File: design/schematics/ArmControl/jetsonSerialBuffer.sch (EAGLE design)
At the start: 7 parts, among them T1 2N3904, T2 2N3904

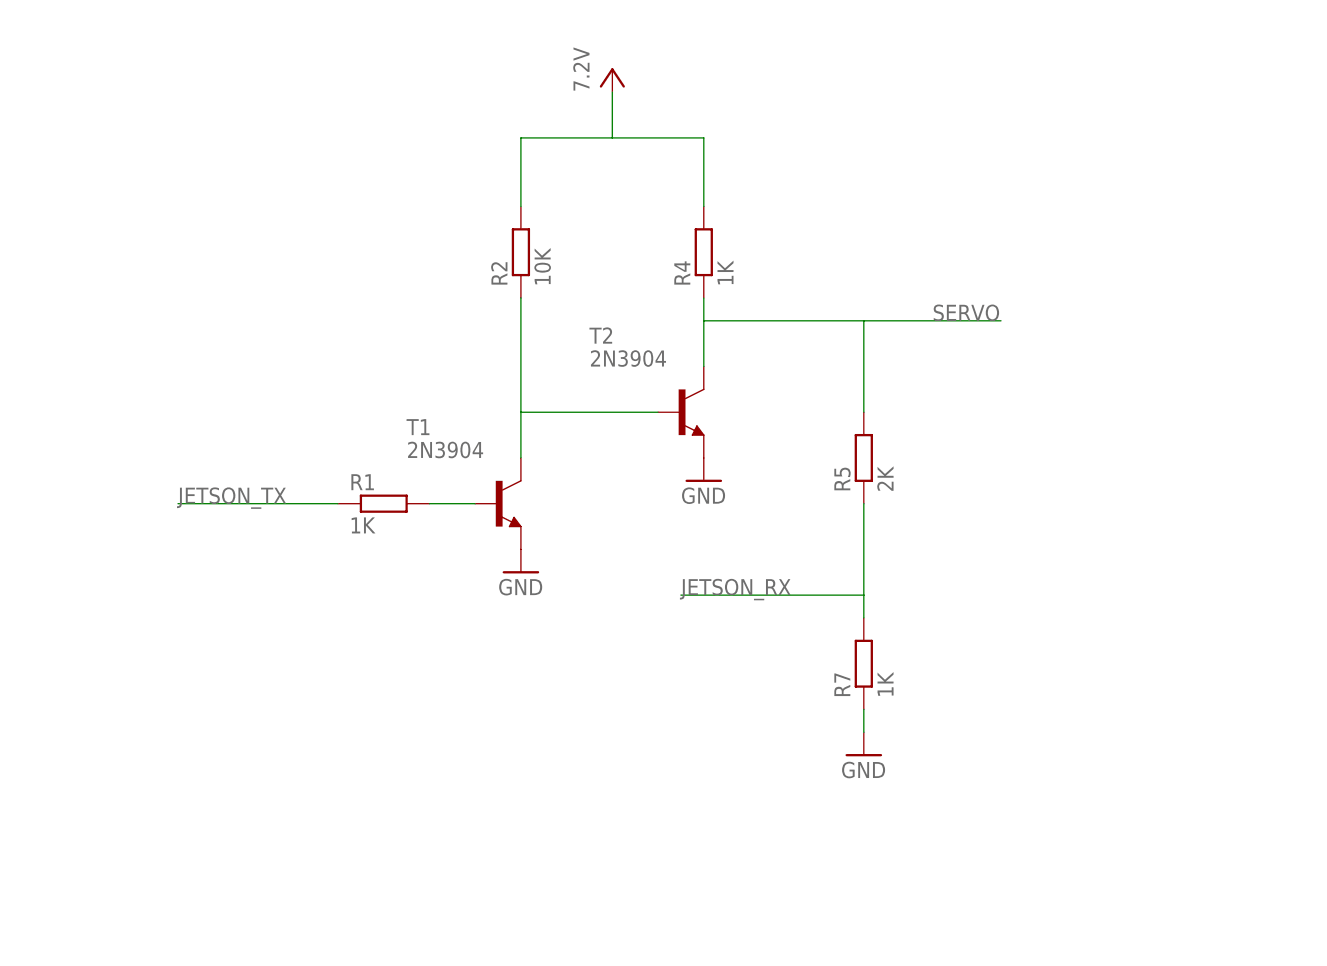
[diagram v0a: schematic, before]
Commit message: updated repo to match current impl
added schematics and pictures
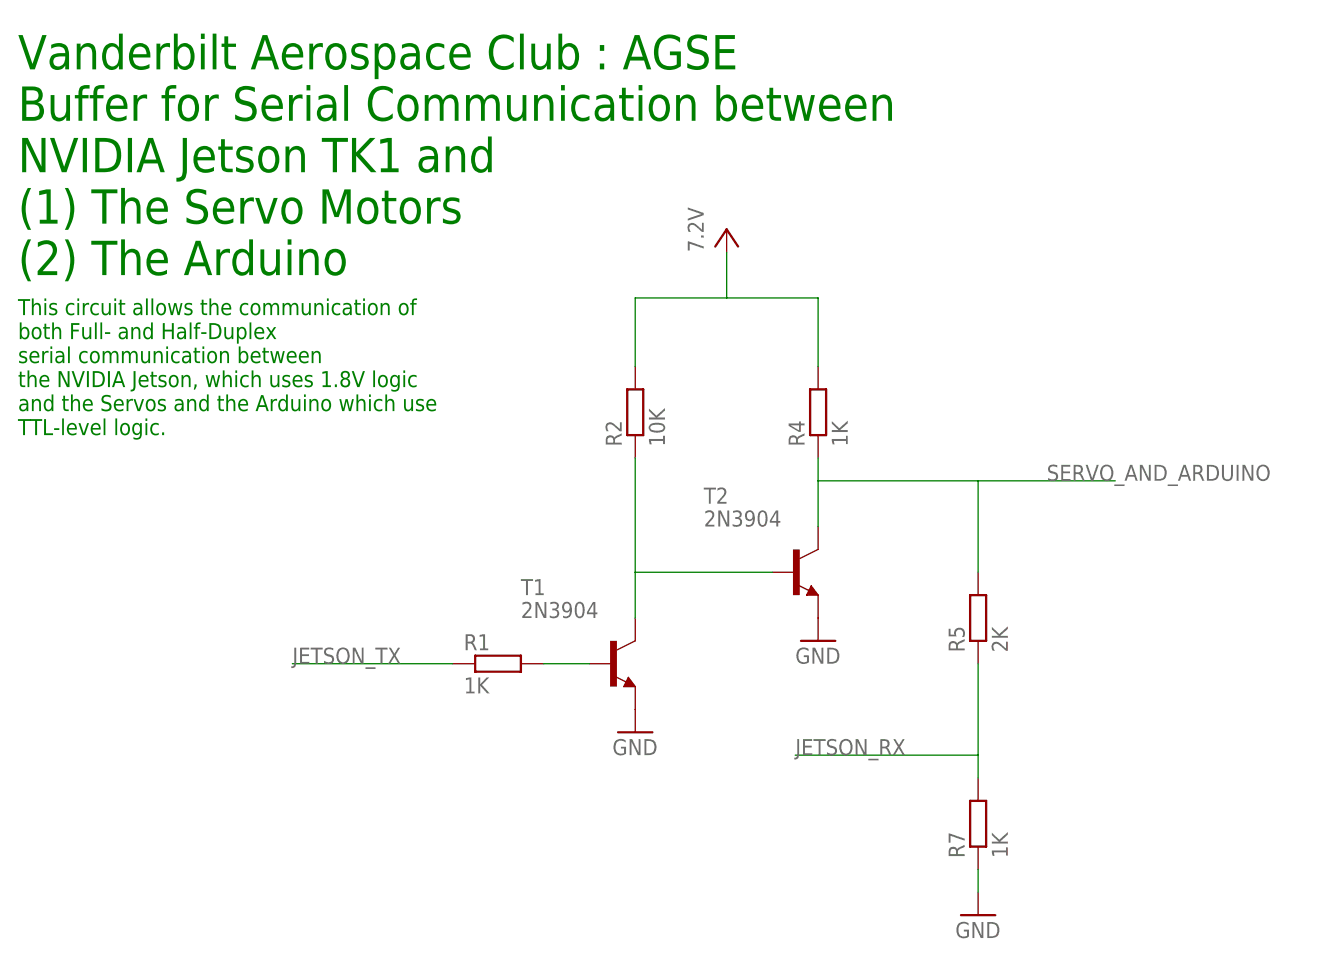
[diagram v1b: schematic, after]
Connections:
- net SERVO renamed SERVO_AND_ARDUINO
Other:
- note added: "This circuit allows the communication of both Full- and Half-Duplex serial communication between the NVIDIA Jetson, which uses 1.8V logic and the Servos and the Arduino which use TTL-level logic."
- note added: "Vanderbilt Aerospace Club : AGSE Buffer for Serial Communication between NVIDIA Jetson TK1 and (1) The Servo Motors (2) The Arduino"
- moved on the sheet: R1, R2, R4, R5, R7, T1, T2
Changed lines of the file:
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@@
 <sheet>
 <plain>
+<text x="10.16" y="99.06" size="3.81" layer="91">Vanderbilt Aerospace Club : AGSE
+Buffer for Serial Communication between
+NVIDIA Jetson TK1 and
+(1) The Servo Motors
+(2) The Arduino</text>
+<text x="10.16" y="81.28" size="1.778" layer="91">This circuit allows the communication of
+both Full- and Half-Duplex
+serial communication between
+the NVIDIA Jetson, which uses 1.8V logic
+and the Servos and the Arduino which use
+TTL-level logic.</text>
 </plain>
 <instances>
-<instance part="T1" gate="G1" x="63.5" y="73.66"/>
-<instance part="T2" gate="G1" x="83.82" y="83.82"/>
-<instance part="R1" gate="G$1" x="50.8" y="73.66"/>
-<instance part="GND1" gate="1" x="66.04" y="66.04"/>
-<instance part="P+1" gate="VCC" x="76.2" y="121.92"/>
-<instance part="R2" gate="G$1" x="66.04" y="101.6" rot="R90"/>
-<instance part="R4" gate="G$1" x="86.36" y="101.6" rot="R90"/>
-<instance part="R5" gate="G$1" x="104.14" y="78.74" rot="R90"/>
-<instance part="R7" gate="G$1" x="104.14" y="55.88" rot="R90"/>
-<instance part="GND3" gate="1" x="86.36" y="76.2"/>
-<instance part="GND4" gate="1" x="104.14" y="45.72"/>
+<instance part="T1" gate="G1" x="76.2" y="55.88"/>
+<instance part="T2" gate="G1" x="96.52" y="66.04"/>
+<instance part="R1" gate="G$1" x="63.5" y="55.88"/>
+<instance part="GND1" gate="1" x="78.74" y="48.26"/>
+<instance part="P+1" gate="VCC" x="88.9" y="104.14"/>
+<instance part="R2" gate="G$1" x="78.74" y="83.82" rot="R90"/>
+<instance part="R4" gate="G$1" x="99.06" y="83.82" rot="R90"/>
+<instance part="R5" gate="G$1" x="116.84" y="60.96" rot="R90"/>
+<instance part="R7" gate="G$1" x="116.84" y="38.1" rot="R90"/>
+<instance part="GND3" gate="1" x="99.06" y="58.42"/>
+<instance part="GND4" gate="1" x="116.84" y="27.94"/>
 <instance part="FRAME2" gate="G$1" x="0" y="0"/>
 </instances>
@@
 <pinref part="T1" gate="G1" pin="B"/>
 <pinref part="R1" gate="G$1" pin="2"/>
-<wire x1="55.88" y1="73.66" x2="60.96" y2="73.66" width="0.1524" layer="91"/>
+<wire x1="68.58" y1="55.88" x2="73.66" y2="55.88" width="0.1524" layer="91"/>
 </segment>
 </net>
@@
 <pinref part="R7" gate="G$1" pin="1"/>
 <pinref part="GND4" gate="1" pin="GND"/>
-<wire x1="104.14" y1="48.26" x2="104.14" y2="50.8" width="0.1524" layer="91"/>
+<wire x1="116.84" y1="30.48" x2="116.84" y2="33.02" width="0.1524" layer="91"/>
 </segment>
 </net>
@@
 <segment>
 <pinref part="R1" gate="G$1" pin="1"/>
-<wire x1="45.72" y1="73.66" x2="27.94" y2="73.66" width="0.1524" layer="91"/>
-<label x="27.94" y="73.66" size="1.778" layer="95"/>
+<wire x1="58.42" y1="55.88" x2="40.64" y2="55.88" width="0.1524" layer="91"/>
+<label x="40.64" y="55.88" size="1.778" layer="95"/>
 </segment>
 </net>
@@
 <pinref part="T1" gate="G1" pin="C"/>
 <pinref part="R2" gate="G$1" pin="1"/>
-<wire x1="66.04" y1="96.52" x2="66.04" y2="83.82" width="0.1524" layer="91"/>
-<wire x1="66.04" y1="83.82" x2="66.04" y2="78.74" width="0.1524" layer="91"/>
-<wire x1="66.04" y1="83.82" x2="81.28" y2="83.82" width="0.1524" layer="91"/>
+<wire x1="78.74" y1="78.74" x2="78.74" y2="66.04" width="0.1524" layer="91"/>
+<wire x1="78.74" y1="66.04" x2="78.74" y2="60.96" width="0.1524" layer="91"/>
+<wire x1="78.74" y1="66.04" x2="93.98" y2="66.04" width="0.1524" layer="91"/>
 <pinref part="T2" gate="G1" pin="B"/>
 </segment>
@@
 <pinref part="P+1" gate="VCC" pin="VCC"/>
 <pinref part="R2" gate="G$1" pin="2"/>
-<wire x1="66.04" y1="106.68" x2="66.04" y2="114.3" width="0.1524" layer="91"/>
-<wire x1="66.04" y1="114.3" x2="76.2" y2="114.3" width="0.1524" layer="91"/>
-<wire x1="76.2" y1="114.3" x2="76.2" y2="119.38" width="0.1524" layer="91"/>
+<wire x1="78.74" y1="88.9" x2="78.74" y2="96.52" width="0.1524" layer="91"/>
+<wire x1="78.74" y1="96.52" x2="88.9" y2="96.52" width="0.1524" layer="91"/>
+<wire x1="88.9" y1="96.52" x2="88.9" y2="101.6" width="0.1524" layer="91"/>
 <pinref part="R4" gate="G$1" pin="2"/>
-<wire x1="76.2" y1="114.3" x2="86.36" y2="114.3" width="0.1524" layer="91"/>
-<wire x1="86.36" y1="114.3" x2="86.36" y2="106.68" width="0.1524" layer="91"/>
+<wire x1="88.9" y1="96.52" x2="99.06" y2="96.52" width="0.1524" layer="91"/>
+<wire x1="99.06" y1="96.52" x2="99.06" y2="88.9" width="0.1524" layer="91"/>
 </segment>
 </net>
@@
 <segment>
 <pinref part="R7" gate="G$1" pin="2"/>
-<wire x1="104.14" y1="73.66" x2="104.14" y2="63.5" width="0.1524" layer="91"/>
-<wire x1="104.14" y1="63.5" x2="104.14" y2="60.96" width="0.1524" layer="91"/>
-<wire x1="104.14" y1="63.5" x2="83.82" y2="63.5" width="0.1524" layer="91"/>
-<label x="83.82" y="63.5" size="1.778" layer="95"/>
+<wire x1="116.84" y1="55.88" x2="116.84" y2="45.72" width="0.1524" layer="91"/>
+<wire x1="116.84" y1="45.72" x2="116.84" y2="43.18" width="0.1524" layer="91"/>
+<wire x1="116.84" y1="45.72" x2="96.52" y2="45.72" width="0.1524" layer="91"/>
+<label x="96.52" y="45.72" size="1.778" layer="95"/>
 <pinref part="R5" gate="G$1" pin="1"/>
 </segment>
 </net>
-<net name="SERVO" class="0">
+<net name="SERVO_AND_ARDUINO" class="0">
 <segment>
 <pinref part="R4" gate="G$1" pin="1"/>
 <pinref part="T2" gate="G1" pin="C"/>
-<wire x1="86.36" y1="96.52" x2="86.36" y2="93.98" width="0.1524" layer="91"/>
+<wire x1="99.06" y1="78.74" x2="99.06" y2="76.2" width="0.1524" layer="91"/>
 <pinref part="R5" gate="G$1" pin="2"/>
-<wire x1="86.36" y1="93.98" x2="86.36" y2="88.9" width="0.1524" layer="91"/>
-<wire x1="104.14" y1="83.82" x2="104.14" y2="93.98" width="0.1524" layer="91"/>
-<wire x1="104.14" y1="93.98" x2="86.36" y2="93.98" width="0.1524" layer="91"/>
-<wire x1="104.14" y1="93.98" x2="119.38" y2="93.98" width="0.1524" layer="91"/>
-<label x="111.76" y="93.98" size="1.778" layer="95"/>
+<wire x1="99.06" y1="76.2" x2="99.06" y2="71.12" width="0.1524" layer="91"/>
+<wire x1="116.84" y1="66.04" x2="116.84" y2="76.2" width="0.1524" layer="91"/>
+<wire x1="116.84" y1="76.2" x2="99.06" y2="76.2" width="0.1524" layer="91"/>
+<wire x1="116.84" y1="76.2" x2="132.08" y2="76.2" width="0.1524" layer="91"/>
+<label x="124.46" y="76.2" size="1.778" layer="95"/>
 </segment>
 </net>
@@
 </schematic>
 </drawing>
+<compatibility>
+<note version="6.3" minversion="6.2.2" severity="warning">
+Since Version 6.2.2 text objects can contain more than one line,
+which will not be processed correctly with this version.
+</note>
+</compatibility>
 </eagle>
